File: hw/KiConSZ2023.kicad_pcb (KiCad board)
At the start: 4 copper layers, 100 x 59.9 mm, 105 parts, among them J2 Conn_01x06, J3 USB_C_Receptacle_USB2.0, J4 Conn_02x03_Top_Bottom, J5 Conn_02x03_Top_Bottom, J6 BM20B(0.8)-10DS-0.4V, Q10 2N7002T, Q11 2N7002T, Q12 2N7002T, Q13 2N7002T, Q14 2N7002T, Q15 2N7002T, Q16 2N7002T, Q2 2N7002T, Q3 2N7002T, Q4 2N7002T, Q5 2N7002T, Q6 2N7002T, Q7 2N7002T, Q8 2N7002T, Q9 2N7002T, SW2 SKRPACE010, SW3 SKRPACE010, SW4 SW_SPDT, U2 N32L406RBL7, U3 PUSB3FR4, U4 AP3410K, U5 BL8536CB3xx

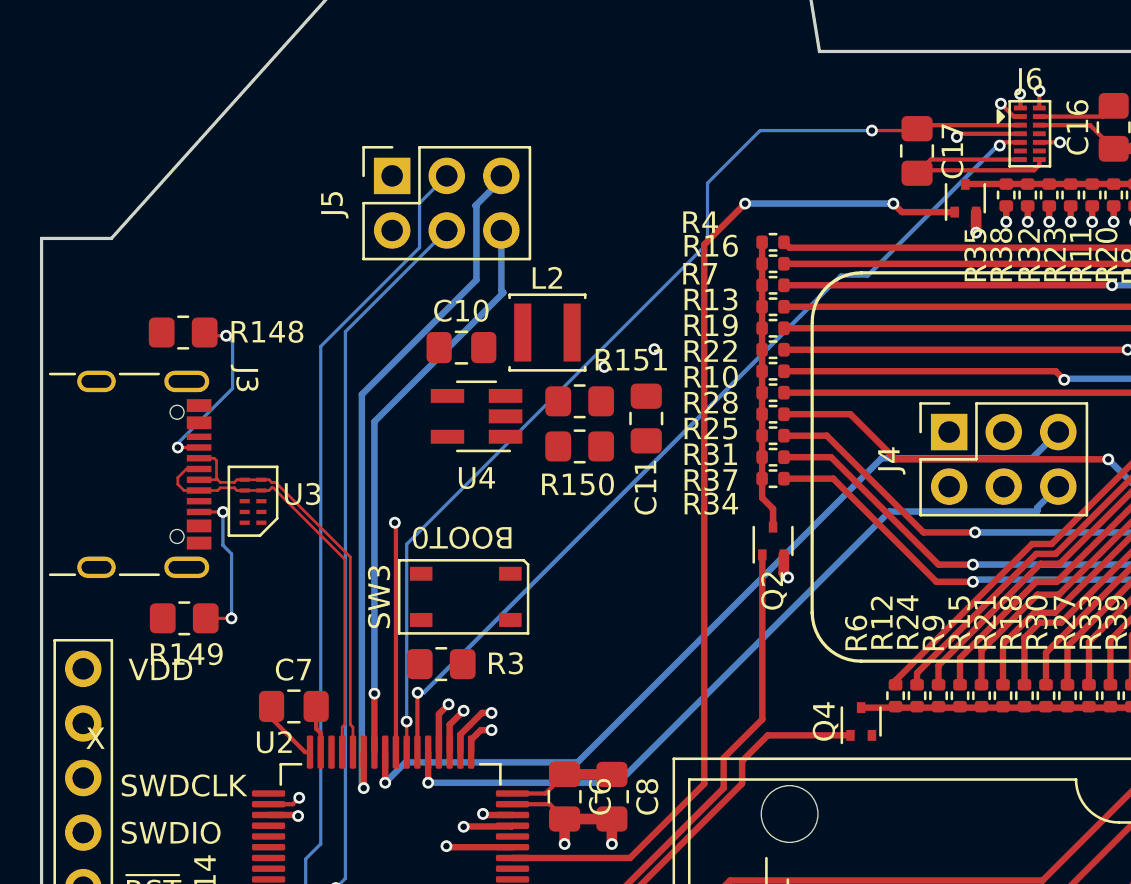
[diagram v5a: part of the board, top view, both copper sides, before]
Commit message: routed (USB) Buck DCDC
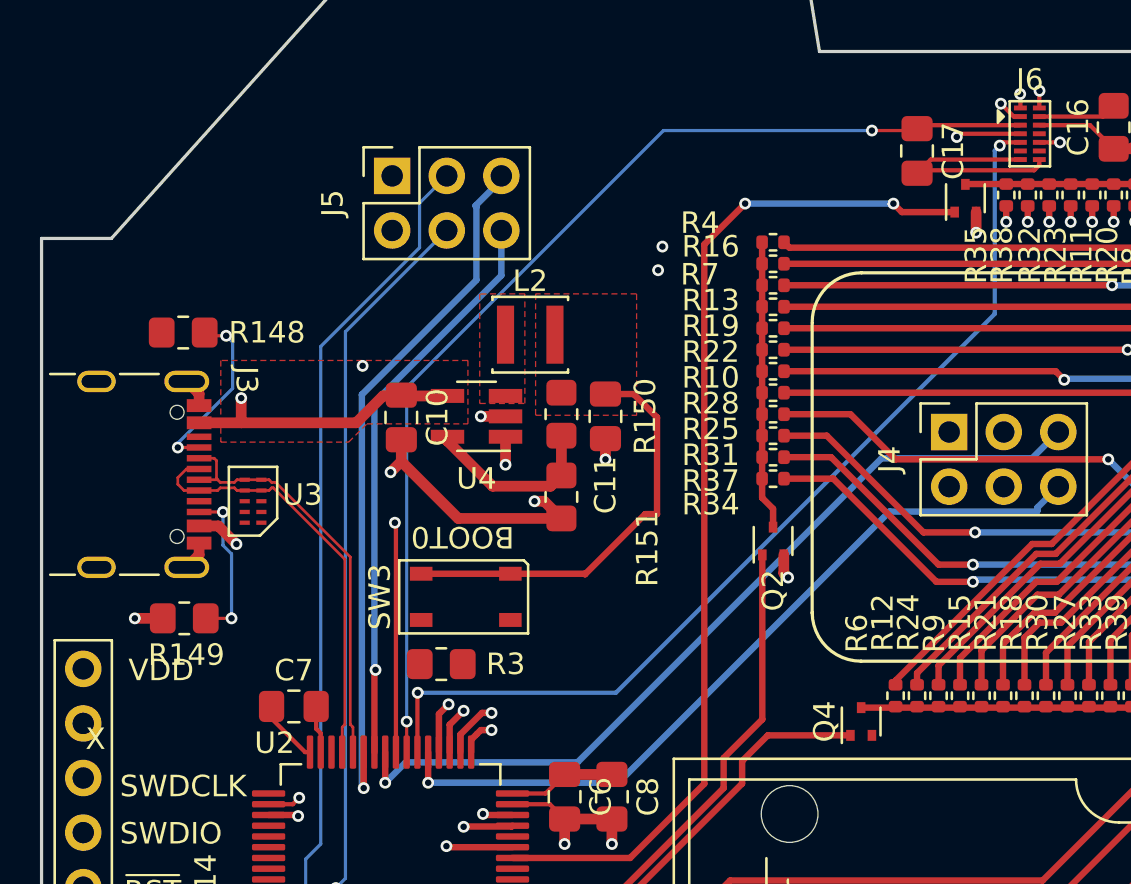
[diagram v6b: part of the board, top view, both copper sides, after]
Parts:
- moved C10 4.29 mm to (67.0, 106.5), turned to -90 degrees
- moved R151 2.50 mm to (74.5, 110.2), turned to -90 degrees
- moved C11 1.90 mm to (76.5, 106.4)
- moved R150 1.04 mm to (74.5, 106.3), turned to -90 degrees
- moved L2 0.81 mm to (73.0, 102.6)
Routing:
- net /VBUS: track 0.00 -> 32.1 mm, vias 0 -> 4
- net VDD: track 67.4 -> 86.8 mm
- net GND: track 50.7 -> 68.7 mm, vias 15 -> 20
- net Net-(U4-FB): track 0.00 -> 8.43 mm
- net /DISP_SCK: track 41.4 -> 45.9 mm
- net /DISP_DISP: track 48.0 -> 50.6 mm
- added copper zone on F.Cu, net /Power/Buck DCDC to 3.3V/LX
- added copper zone on F.Cu, net /VBUS
- added copper zone on F.Cu, net VDD

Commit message: put VDD zone
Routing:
- net /DISP_SCK: track 45.9 -> 49.3 mm
- net VDD: track 86.8 -> 85.2 mm, vias 0 -> 2
- added copper zone on B.Cu, net VDD
- added copper zone on In2.Cu, net VDD
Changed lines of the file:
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@@
   (via (at 67.761696 119.261696) (size 0.55) (drill 0.3) (layers "F.Cu" "B.Cu") (net 39))
   (via (at 94.85 93.8) (size 0.55) (drill 0.3) (layers "F.Cu" "B.Cu") (net 39))
-  (segment (start 67.761696 119.261696) (end 76.988304 119.261696) (width 0.2) (layer "B.Cu") (net 39))
+  (segment (start 79.465 94.035) (end 94.615 94.035) (width 0.2) (layer "B.Cu") (net 39))
   (segment (start 94.615 94.035) (end 94.85 93.8) (width 0.2) (layer "B.Cu") (net 39))
-  (segment (start 94.615 101.635) (end 94.615 94.035) (width 0.2) (layer "B.Cu") (net 39))
-  (segment (start 76.988304 119.261696) (end 94.615 101.635) (width 0.2) (layer "B.Cu") (net 39))
+  (segment (start 67.761696 119.261696) (end 67.761696 105.738304) (width 0.2) (layer "B.Cu") (net 39))
+  (segment (start 67.761696 105.738304) (end 79.465 94.035) (width 0.2) (layer "B.Cu") (net 39))
   (segment (start 96.69 93.65) (end 97.65 93.65) (width 0.2) (layer "F.Cu") (net 42))
   (segment (start 66.75 111.4) (end 66.75 122.025) (width 0.2) (layer "F.Cu") (net 42))
@@
   (segment (start 64.4 127.9) (end 64.4 102.465) (width 0.15) (layer "B.Cu") (net 120))
   (segment (start 73.7125 123.95) (end 74.6 123.0625) (width 0.2) (layer "F.Cu") (net 123))
-  (segment (start 78.35 110.95) (end 75.55 113.75) (width 0.3) (layer "F.Cu") (net 123))
   (segment (start 56.148286 132.2375) (end 55.492893 132.892893) (width 0.15) (layer "F.Cu") (net 123))
-  (segment (start 78.9 110.95) (end 78.35 110.95) (width 0.3) (layer "F.Cu") (net 123))
   (segment (start 99.05 92.85) (end 100.15 93.95) (width 0.2) (layer "F.Cu") (net 123))
-  (segment (start 77.8125 105.3625) (end 78.9 106.45) (width 0.3) (layer "F.Cu") (net 123))
   (segment (start 73.5375 130.2625) (end 74.9 130.2625) (width 0.2) (layer "F.Cu") (net 123))
   (segment (start 73.35 130.45) (end 73.5375 130.2625) (width 0.2) (layer "F.Cu") (net 123))
   (segment (start 121.755 92.155) (end 132.9 92.155) (width 0.5) (layer "F.Cu") (net 123))
+  (segment (start 75.525 113.725) (end 72.075 113.725) (width 0.3) (layer "F.Cu") (net 123))
   (segment (start 60.825 131.45) (end 58.9875 131.45) (width 0.2) (layer "F.Cu") (net 123))
   (segment (start 68.75 134.85) (end 69.3375 135.4375) (width 0.2) (layer "F.Cu") (net 123))
   (segment (start 132.9 92.155) (end 137.4 92.155) (width 0.5) (layer "F.Cu") (net 123))
+  (segment (start 78.35 110.9) (end 75.525 113.725) (width 0.3) (layer "F.Cu") (net 123))
   (segment (start 72.075 113.725) (end 67.925 113.725) (width 0.3) (layer "F.Cu") (net 123))
   (segment (start 68.75 133.375) (end 68.75 134.85) (width 0.2) (layer "F.Cu") (net 123))
   (segment (start 69.3375 135.4375) (end 69.3375 136.6) (width 0.2) (layer "F.Cu") (net 123))
   (segment (start 72.175 130.45) (end 73.35 130.45) (width 0.2) (layer "F.Cu") (net 123))
-  (segment (start 75.55 113.75) (end 75.525 113.725) (width 0.3) (layer "F.Cu") (net 123))
-  (segment (start 76.5 105.3625) (end 77.8125 105.3625) (width 0.3) (layer "F.Cu") (net 123))
+  (segment (start 78.35 107.2125) (end 78.35 110.9) (width 0.3) (layer "F.Cu") (net 123))
+  (segment (start 76.5 105.3625) (end 78.35 107.2125) (width 0.3) (layer "F.Cu") (net 123))
   (segment (start 72.175 123.95) (end 73.7125 123.95) (width 0.2) (layer "F.Cu") (net 123))
   (segment (start 69.3375 136.6) (end 71.1625 136.6) (width 0.5) (layer "F.Cu") (net 123))
@@
   (segment (start 58.9875 131.45) (end 58.2 132.2375) (width 0.2) (layer "F.Cu") (net 123))
   (segment (start 115.1 90.555) (end 120.155 90.555) (width 0.5) (layer "F.Cu") (net 123))
-  (segment (start 78.9 106.45) (end 78.9 110.95) (width 0.3) (layer "F.Cu") (net 123))
   (segment (start 120.155 90.555) (end 121.755 92.155) (width 0.5) (layer "F.Cu") (net 123))
   (segment (start 96.69 92.85) (end 99.05 92.85) (width 0.2) (layer "F.Cu") (net 123))
-  (segment (start 75.525 113.725) (end 72.075 113.725) (width 0.3) (layer "F.Cu") (net 123))
   (segment (start 58.2 132.2375) (end 56.148286 132.2375) (width 0.15) (layer "F.Cu") (net 123))
+  (via (at 76.4 101.4) (size 0.55) (drill 0.3) (layers "F.Cu" "B.Cu") (free) (net 123))
+  (via (at 76.4 103) (size 0.55) (drill 0.3) (layers "F.Cu" "B.Cu") (free) (net 123))
   (zone (net 44) (net_name "/Power/Buck DCDC to 3.3V/LX") (layer "F.Cu") (name "LX") (hatch edge 0.5)
     (priority 22)
@@
         (xy 72.75 105.8)
         (xy 72.75 100.7)
-      )
-    )
-  )
-  (zone (net 123) (net_name "VDD") (layer "F.Cu") (name "BUCK_VDD") (hatch edge 0.5)
-    (priority 25)
-    (connect_pads (clearance 0.1))
-    (min_thickness 0.2) (filled_areas_thickness no)
-    (fill yes (thermal_gap 0.2) (thermal_bridge_width 0.5))
-    (polygon
-      (pts
-        (xy 73.25 100.7)
-        (xy 73.25 106.35)
-        (xy 77.95 106.35)
-        (xy 77.95 100.7)
       )
     )
@@
     )
   )
+  (zone (net 123) (net_name "VDD") (layers "F.Cu" "In2.Cu" "B.Cu") (name "BUCK_VDD") (hatch edge 0.5)
+    (priority 30)
+    (connect_pads (clearance 0.1))
+    (min_thickness 0.2) (filled_areas_thickness no)
+    (fill yes (thermal_gap 0.2) (thermal_bridge_width 0.5))
+    (polygon
+      (pts
+        (xy 73.25 100.7)
+        (xy 73.25 106.35)
+        (xy 77.95 106.35)
+        (xy 77.95 100.7)
+      )
+    )
+  )
   (zone (net 2) (net_name "GND") (layer "In1.Cu") (name "BUCK_GND") (hatch edge 0.5)
     (priority 20)
@@
       )
     )
+  )
+  (zone (net 123) (net_name "VDD") (layers "In2.Cu" "B.Cu") (name "VDD") (hatch edge 0.5)
+    (priority 35)
+    (connect_pads (clearance 0.1))
+    (min_thickness 0.25) (filled_areas_thickness no)
+    (fill yes (thermal_gap 0.5) (thermal_bridge_width 0.5))
+    (polygon
+      (pts
+        (xy 74.65 100.7)
+        (xy 74.65 106.35)
+        (xy 77.95 106.35)
+        (xy 77.95 100.7)
+      )
+    )

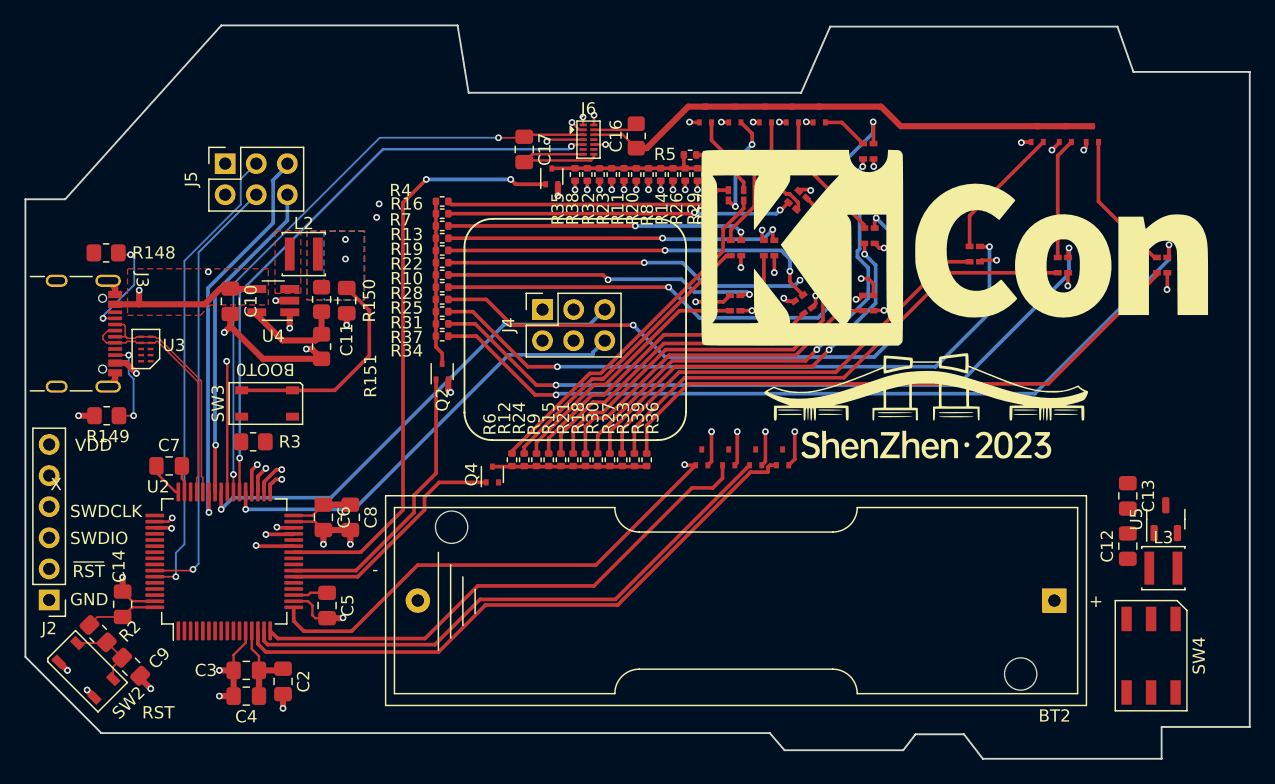
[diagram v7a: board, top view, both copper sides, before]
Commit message: routed most VDD
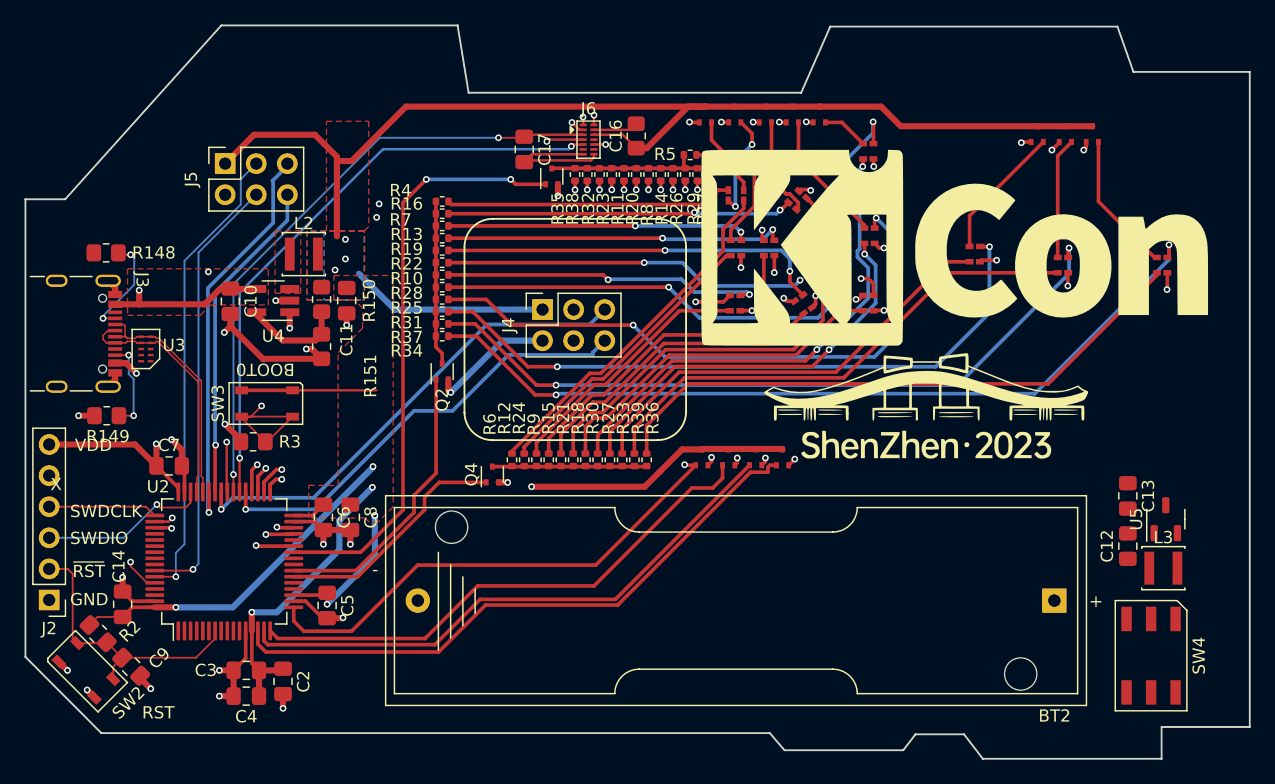
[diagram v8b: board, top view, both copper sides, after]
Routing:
- net VDD: track 85.2 -> 248.1 mm, vias 2 -> 11
- net /MCU/BOOT0: track 0.00 -> 32.1 mm, vias 0 -> 2
- net /MCU/~{RST}: track 6.27 -> 23.0 mm
- net GND: track 68.7 -> 82.7 mm, vias 20 -> 23
- net /MCU/SWDIO: track 0.00 -> 13.8 mm, vias 0 -> 1
- net /MCU/SWDCLK: track 0.00 -> 8.92 mm
- net /DISP_MOSI: track 50.9 -> 47.6 mm
- net /SAO_SCL: track 66.8 -> 69.4 mm
- net /SAO_SDA: track 69.1 -> 71.0 mm
